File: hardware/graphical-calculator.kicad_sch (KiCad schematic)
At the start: 43 parts, among them SW0 SW_Omron_B3FS, SW1 SW_Omron_B3FS, SW2 SW_Omron_B3FS, SW3 SW_Omron_B3FS, SW4 SW_Omron_B3FS, SW5 SW_Omron_B3FS, SW6 SW_Omron_B3FS, SW7 SW_Omron_B3FS, SW8 SW_Omron_B3FS, SW9 SW_Omron_B3FS, U1 RASPBERRY_PI_ZERO_2_W, U4 MCP23017_SO, U5 MCP23017_SO

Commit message: update pcb and 3d model
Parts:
- removed SWZOOM1: SW_Push_SPDT, Button_Switch_SMD:SW_SPDT_CK_JS102011SAQN, symbol Switch:SW_Push_SPDT
- added SWIN1, SWOUT1: SW_Omron_B3FS, Button_Switch_SMD:SW_SPST_Omron_B3FS-105xP, symbol Switch:SW_Omron_B3FS
- SW0, SW1, SW2, SW3, SW4, SW5, SW6, SW7, SW8, SW9, SWAC1, SWCOS1, SWDEL1, SWDIV1, SWDOT1, SWDOWN1, SWEXE1, SWFRAC1, SWINT1, SWLBRAC1, SWLEFT1, SWLN1, SWLOG1, SWMINUS1, SWMULT1, SWON1, SWPI1, SWPLUS1, SWPOWER1, SWRBRAC1, SWRIGHT1, SWSHIFT1, SWSIN1, SWSQRT1, SWSQUARE1, SWTAN1, SWUP1, SWX1: LCSC (none) -> C306879
- SWRAD1: footprint Button_Switch_SMD:SW_SPDT_CK_JS102011SAQN -> JS102011JCQN:SW_JS102011JCQN; symbol Switch:SW_SPDT -> JS102011CQN:JS102011CQN; Arrow Part Number (none) -> JS102011CQN; Arrow Price/Stock (none) -> https://www.arrow.com/en/products/js102011cqn/ck?utm_curren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; Height (none) -> 5.5; LCSC (none) -> C221659; Manufacturer_Name (none) -> C & K COMPONENTS; Manufacturer_Part_Number (none) -> JS102011CQN; Mouser Part Number (none) -> 611-JS102011CQN; Mouser Price/Stock (none) -> https://www.mouser.co.uk/ProductDetail/CK/js102011cqn?qs=j%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
- U4, U5: LCSC (none) -> C47023
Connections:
- net DEG: now also SWRAD1.1 (NC); no longer SWRAD1.2 (B)
- net GND: now also SWRAD1.2 (COM), SWIN1.2, SWOUT1.2; no longer SWRAD1.3 (C)
- net IN: now also SWIN1.1
- net OUT: now also SWOUT1.1
- net RAD: now also SWRAD1.3 (NO); no longer SWRAD1.1 (A)

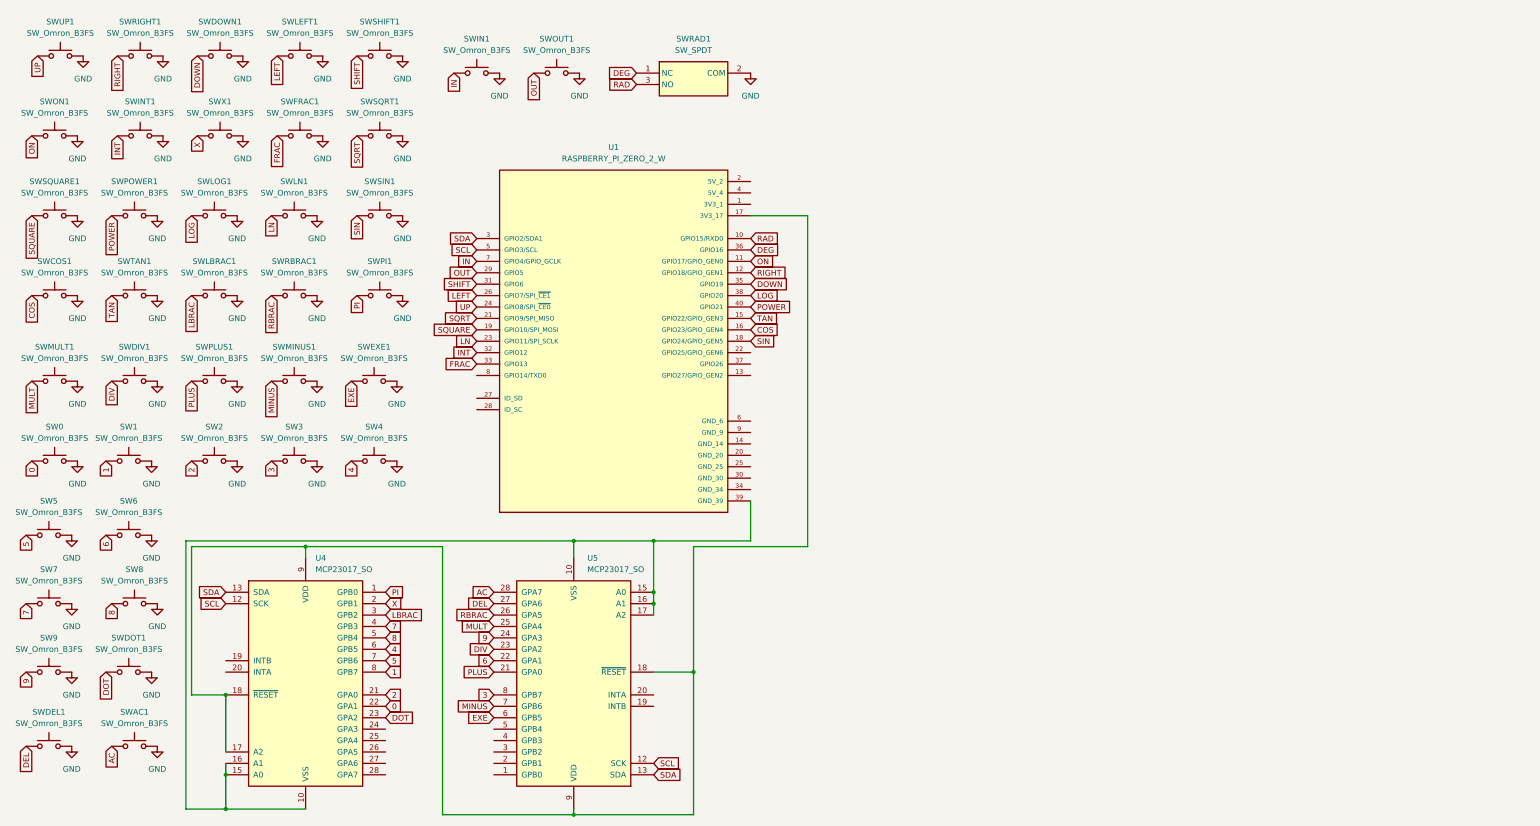
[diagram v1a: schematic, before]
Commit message: redo board with matrix, tht, cad with screen
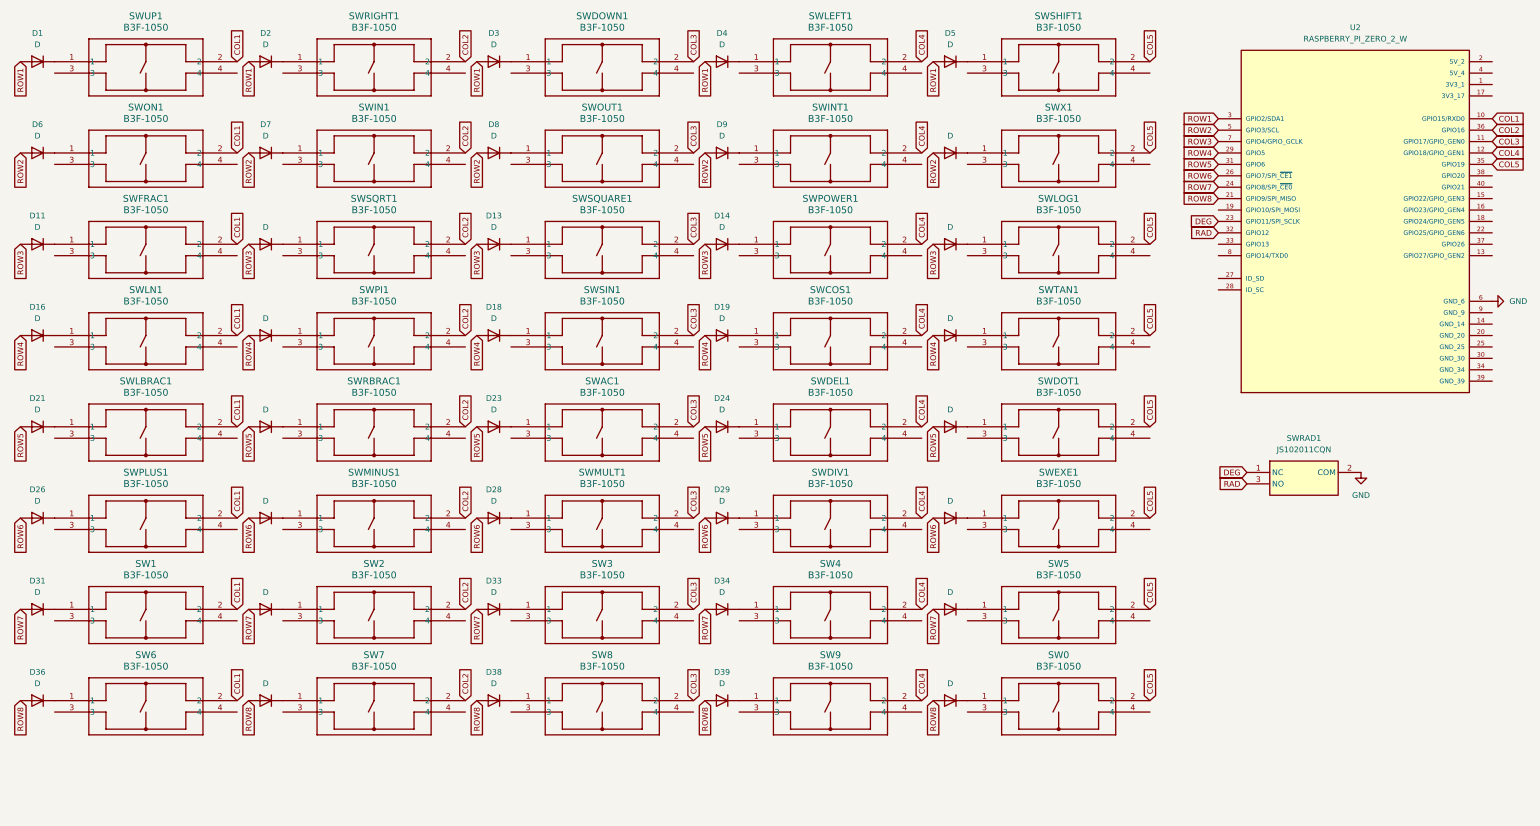
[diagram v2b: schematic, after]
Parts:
- removed SW0, SW1, SW2, SW3, SW4, SW5, SW6, SW7, SW8, SW9, SWAC1, SWCOS1, SWDEL1, SWDIV1, SWDOT1, SWDOWN1, SWEXE1, SWFRAC1, SWIN1, SWINT1, SWLBRAC1, SWLEFT1, SWLN1, SWLOG1, SWMINUS1, SWMULT1, SWON1, SWOUT1, SWPI1, SWPLUS1, SWPOWER1, SWRBRAC1, SWRIGHT1, SWSHIFT1, SWSIN1, SWSQRT1, SWSQUARE1, SWTAN1, SWUP1, SWX1: SW_Omron_B3FS, Button_Switch_SMD:SW_SPST_Omron_B3FS-105xP, symbol Switch:SW_Omron_B3FS
- removed U1: RASPBERRY_PI_ZERO_2_W, RPI_Zero2W:MODULE_RASPBERRY_PI_ZERO_2_W, symbol RASPBERRY_PI_ZERO_2_W:RASPBERRY_PI_ZERO_2_W
- removed U4, U5: MCP23017_SO, Package_SO:SOIC-28W_7.5x17.9mm_P1.27mm, symbol Interface_Expansion:MCP23017_SO
- added D1, D10, D11, D12, D13, D14, D15, D16, D17, D18, D19, D2, D20, D21, D22, D23, D24, D25, D26, D27, D28, D29, D3, D30, D31, D32, D33, D34, D35, D36, D37, D38, D39, D4, D40, D5, D6, D7, D8, D9: D, 1N4148 _DO-35_:DIOAD1300W80L670D310, symbol Device:D
- added SW0, SW1, SW2, SW3, SW4, SW5, SW6, SW7, SW8, SW9, SWAC1, SWCOS1, SWDEL1, SWDIV1, SWDOT1, SWDOWN1, SWEXE1, SWFRAC1, SWIN1, SWINT1, SWLBRAC1, SWLEFT1, SWLN1, SWLOG1, SWMINUS1, SWMULT1, SWON1, SWOUT1, SWPI1, SWPLUS1, SWPOWER1, SWRBRAC1, SWRIGHT1, SWSHIFT1, SWSIN1, SWSQRT1, SWSQUARE1, SWTAN1, SWUP1, SWX1: B3F-1050, B3F-1050:SW_B3F-1050_OMR, symbol B3F-1050:B3F-1050
- added U2: RASPBERRY_PI_ZERO_2_W, RPI-Zero-2W:MODULE_RASPBERRY_PI_ZERO_2_W, symbol RASPBERRY_PI_ZERO_2_W:RASPBERRY_PI_ZERO_2_W
- SWRAD1: value SW_SPDT -> JS102011CQN; footprint JS102011JCQN:SW_JS102011JCQN -> JS102011CQN:JS102011CQN; LCSC C221659 -> (none)
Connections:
- net DEG: now also U2.23 (GPIO11/SPI_SCLK)
- net GND: now also U2.6 (GND_6)
- net RAD: now also U2.32 (GPIO12)
- new net: D33.1 (K), SW3.1
- new net: D39.1 (K), SW9.1
- new net: D31.1 (K), SW1.1
- new net: D8.1 (K), SWOUT1.1
- new net: D18.1 (K), SWSIN1.1
- new net: D13.1 (K), SWSQUARE1.1
- new net: D21.1 (K), SWLBRAC1.1
- new net: D25.1 (K), SWDOT1.1
- new net: D34.1 (K), SW4.1
- new net: D38.1 (K), SW8.1
- new net: D3.1 (K), SWDOWN1.1
- new net: D40.1 (K), SW0.1
- new net: D2.1 (K), SWRIGHT1.1
- new net: D23.1 (K), SWAC1.1
- new net: D29.1 (K), SWDIV1.1
- new net: D37.1 (K), SW7.1
- new net: D36.1 (K), SW6.1
- new net: D24.1 (K), SWDEL1.1
- new net: D30.1 (K), SWEXE1.1
- new net: D12.1 (K), SWSQRT1.1
- new net: D11.1 (K), SWFRAC1.1
- new net: D20.1 (K), SWTAN1.1
- new net: D15.1 (K), SWLOG1.1
- new net: D22.1 (K), SWRBRAC1.1
- new net: D26.1 (K), SWPLUS1.1
- new net: D5.1 (K), SWSHIFT1.1
- new net: D17.1 (K), SWPI1.1
- new net: D9.1 (K), SWINT1.1
- new net: D6.1 (K), SWON1.1
- new net: D14.1 (K), SWPOWER1.1
- new net: D19.1 (K), SWCOS1.1
- new net: D32.1 (K), SW2.1
- new net: D27.1 (K), SWMINUS1.1
- new net: D1.1 (K), SWUP1.1
- new net: D16.1 (K), SWLN1.1
- new net: D28.1 (K), SWMULT1.1
- new net: D10.1 (K), SWX1.1
- new net: D35.1 (K), SW5.1
- new net: D4.1 (K), SWLEFT1.1
- new net: D7.1 (K), SWIN1.1
- new net COL1: SW1.2, SW6.2, SWFRAC1.2, SWLBRAC1.2, SWLN1.2, SWON1.2, SWPLUS1.2, SWUP1.2, U2.10 (GPIO15/RXD0)
- new net COL2: SW2.2, SW7.2, SWIN1.2, SWMINUS1.2, SWPI1.2, SWRBRAC1.2, SWRIGHT1.2, SWSQRT1.2, U2.36 (GPIO16)
- new net COL3: SW3.2, SW8.2, SWAC1.2, SWDOWN1.2, SWMULT1.2, SWOUT1.2, SWSIN1.2, SWSQUARE1.2, U2.11 (GPIO17/GPIO_GEN0)
- new net COL4: SW4.2, SW9.2, SWCOS1.2, SWDEL1.2, SWDIV1.2, SWINT1.2, SWLEFT1.2, SWPOWER1.2, U2.12 (GPIO18/GPIO_GEN1)
- new net COL5: SW0.2, SW5.2, SWDOT1.2, SWEXE1.2, SWLOG1.2, SWSHIFT1.2, SWTAN1.2, SWX1.2, U2.35 (GPIO19)
- new net ROW1: D1.2 (A), D2.2 (A), D3.2 (A), D4.2 (A), D5.2 (A), U2.3 (GPIO2/SDA1)
- new net ROW2: D10.2 (A), D6.2 (A), D7.2 (A), D8.2 (A), D9.2 (A), U2.5 (GPIO3/SCL)
- new net ROW3: D11.2 (A), D12.2 (A), D13.2 (A), D14.2 (A), D15.2 (A), U2.7 (GPIO4/GPIO_GCLK)
- new net ROW4: D16.2 (A), D17.2 (A), D18.2 (A), D19.2 (A), D20.2 (A), U2.29 (GPIO5)
- new net ROW5: D21.2 (A), D22.2 (A), D23.2 (A), D24.2 (A), D25.2 (A), U2.31 (GPIO6)
- new net ROW6: D26.2 (A), D27.2 (A), D28.2 (A), D29.2 (A), D30.2 (A), U2.26 (GPIO7/SPI_~{CE1})
- new net ROW7: D31.2 (A), D32.2 (A), D33.2 (A), D34.2 (A), D35.2 (A), U2.24 (GPIO8/SPI_~{CE0})
- new net ROW8: D36.2 (A), D37.2 (A), D38.2 (A), D39.2 (A), D40.2 (A), U2.21 (GPIO9/SPI_MISO)
